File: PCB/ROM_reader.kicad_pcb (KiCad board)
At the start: 2 copper layers, 94 x 59 mm, 41 parts, among them J1 TTL_UART, J2 USB_B_Mini, J3 ISP, J4 DB25_Plug, M1 MountingHole_3.2mm_M3_DIN965, M2 MountingHole_3.2mm_M3_DIN965, M3 MountingHole_3.2mm_M3_DIN965, M4 MountingHole_3.2mm_M3_DIN965, SW1 RST, U1 CH340G, U2 ATmega128A-A, Y1 12MHz, Y2 12MHz

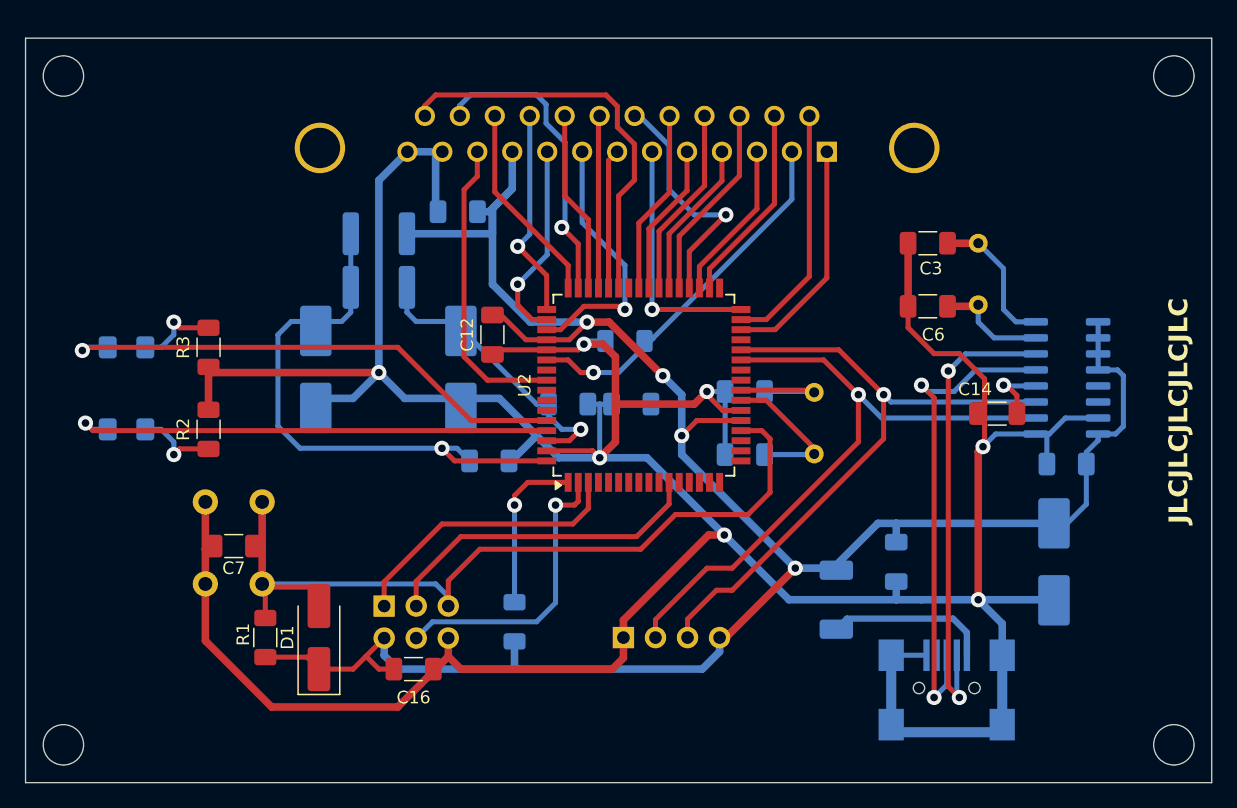
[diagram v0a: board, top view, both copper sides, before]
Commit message: ROM reader project PCBs updated
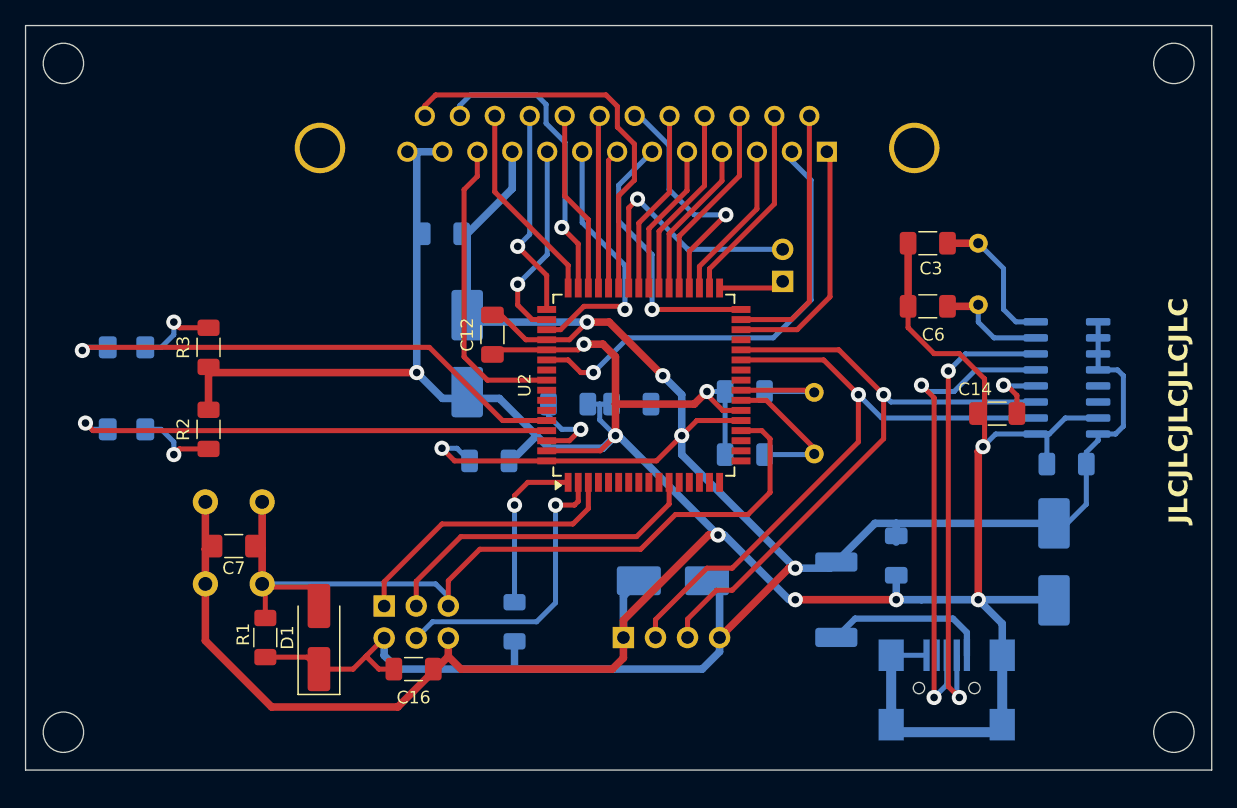
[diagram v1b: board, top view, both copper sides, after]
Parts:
- removed C11: 100u, Capacitor_SMD:CP_Elec_8x5.4
- removed L1, L2: 100u, Inductor_SMD:L_1812_4532Metric_Pad1.30x3.40mm_HandSolder
- removed M1, M2, M3, M4: MountingHole_3.2mm_M3_DIN965, MountingHole:MountingHole_3.2mm_M3_DIN965
- removed R5: 10M, Resistor_SMD:R_1206_3216Metric_Pad1.30x1.75mm_HandSolder
- added D5: Schottky, Diode_SMD:D_SMB_Handsoldering, B.Cu at (143.3, 104.5)
- added H1: MH, MountingHole:MountingHole_3.2mm_M3_DIN965, F.Cu at (95.0, 63.5)
- added H2: MH, MountingHole:MountingHole_3.2mm_M3_DIN965, F.Cu at (183.0, 63.5)
- added H3: MH, MountingHole:MountingHole_3.2mm_M3_DIN965, F.Cu at (183.0, 116.5)
- added H4: MH, MountingHole:MountingHole_3.2mm_M3_DIN965, F.Cu at (95.0, 116.5)
- added J4: EC, Connector_PinHeader_2.54mm:PinHeader_1x02_P2.54mm_Vertical, B.Cu at (152.0, 80.8)
- F1: footprint Fuse:Fuse_2010_5025Metric_Pad1.52x2.65mm_HandSolder -> Fuse:Fuse_2512_6332Metric_Pad1.52x3.35mm_HandSolder
- R2, R3: value 10k -> 1k5
- Y2: value 12MHz -> 7.3782MHz
- moved C8 12.1 mm to (127.0, 86.5)
- moved C4 2.15 mm to (125.0, 77.0)
- moved C9 0.50 mm to (161.0, 102.5)
- renumbered J2 to J1, J1 to J2, J4 to J5
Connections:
- C1 pad 1: +5V -> AVCC
- C12 pad 1: +5V -> AVCC
- C16 pad 1: +5V -> AVCC
- C17 pad 1: +5V -> AVCC
- C2 pad 1: +5V -> AVCC
- C4 pad 1: +5V -> AVCC
- C9 pad 1: +5V -> AVCC
- D1 pad 1: +5V -> AVCC
- F1 pad 2: +5V -> AVCC
- J2 pad 4: +5V -> AVCC
- J3 pad 2: +5V -> AVCC
- J5 pad 10: +5V -> AVCC
- R1 pad 2: +5V -> AVCC
- R4 pad 2: +5V -> AVCC
- U1 pad 10: +5V -> AVCC
- U1 pad 11: +5V -> AVCC
- U1 pad 12: +5V -> AVCC
- U1 pad 16: +5V -> AVCC
- U1 pad 9: +5V -> AVCC
- U2 pad 21: +5V -> AVCC
- U2 pad 33: unconnected-(U2-PG0-Pad33) -> #WR
- U2 pad 42: unconnected-(U2-PC7-Pad42) -> A15_RAM_ADAPTER
- U2 pad 52: +5V -> AVCC
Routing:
- net +5V: track 175.7 -> 0.00 mm, vias 4 -> 0
- net AVCC: track 45.0 -> 195.3 mm, vias 1 -> 5
- net A15_RAM_ADAPTER: track 0.00 -> 20.5 mm, vias 0 -> 1
- net AREF: track 23.2 -> 7.01 mm
- net GND: track 303.8 -> 294.1 mm, vias 7 -> 9
- net /A15: track 30.1 -> 36.1 mm
- net #WR: track 0.00 -> 5.22 mm
- net B+C: track 19.5 -> 21.7 mm
- net B: track 18.5 -> 19.7 mm
- net #A: track 19.5 -> 20.7 mm
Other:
- board text added: "EC"
- board text added: "FLT/ART/CU-1 ROM READER"
- board text added: "FUSE"

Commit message: Minor changes in text placement on PCB, comments. Revision updated to B
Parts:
- D3: renamed from D2; footprint LED_SMD:LED_1206_3216Metric_Pad1.42x1.75mm_HandSolder -> LED_SMD:LED_2010_5025Metric_Pad1.52x2.65mm_HandSolder
- D4: renamed from D3; footprint LED_SMD:LED_1206_3216Metric_Pad1.42x1.75mm_HandSolder -> LED_SMD:LED_2010_5025Metric_Pad1.52x2.65mm_HandSolder
- J4: value EC -> RAM ADAPTER EXT; footprint Connector_PinHeader_2.54mm:PinHeader_1x02_P2.54mm_Vertical -> Connector_PinHeader_2.54mm:PinHeader_1x02_P2.54mm_Horizontal
- J5: value DB25_Plug -> ROM MODULE
- moved J4 24.3 mm to (175.3, 73.9), turned to 90 degrees
- renumbered C12 to C11, C13 to C12, C14 to C13, C15 to C14, C16 to C15, C17 to C16, D5 to D1, D1 to D2, H3 to H2, H2 to H3
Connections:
- net AVCC renamed +5V
- J5 pad 0: (no net) -> GND
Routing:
- net #WR: track 5.22 -> 44.6 mm, vias 0 -> 2
- net A15_RAM_ADAPTER: track 20.5 -> 57.5 mm
- net GND: track 294.1 -> 301.1 mm
- net /A9: track 19.5 -> 17.0 mm
- net Net-(D3-K): track 6.61 -> 5.86 mm
- net Net-(D4-K): track 6.61 -> 5.91 mm
- net Net-(D3-A): track 38.8 -> 39.4 mm
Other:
- board text added: "ADAPTER"
- board text added: "MODULE"
- board text added: "RAM"
- board text added: "ROM"
- board text added: "trwgQ26xxx"
- board text removed: "EC"

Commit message: PCB project update: pull-up resistors added for D0-D7 data lines
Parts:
- added R10: 22k, Resistor_SMD:R_1206_3216Metric_Pad1.30x1.75mm_HandSolder, F.Cu at (134.4, 75.3)
- added R11: 22k, Resistor_SMD:R_1206_3216Metric_Pad1.30x1.75mm_HandSolder, F.Cu at (134.8, 73.0)
- added R12: 22k, Resistor_SMD:R_1206_3216Metric_Pad1.30x1.75mm_HandSolder, B.Cu at (137.8, 78.2)
- added R5: 22k, Resistor_SMD:R_1206_3216Metric_Pad1.30x1.75mm_HandSolder, B.Cu at (137.8, 80.6)
- added R6: 22k, Resistor_SMD:R_1206_3216Metric_Pad1.30x1.75mm_HandSolder, B.Cu at (133.4, 81.4)
- added R7: 22k, Resistor_SMD:R_1206_3216Metric_Pad1.30x1.75mm_HandSolder, B.Cu at (129.2, 78.4)
- added R8: 22k, Resistor_SMD:R_1206_3216Metric_Pad1.30x1.75mm_HandSolder, F.Cu at (129.0, 78.3)
- added R9: 22k, Resistor_SMD:R_1206_3216Metric_Pad1.30x1.75mm_HandSolder, F.Cu at (124.8, 73.0)
- R2, R3: value 1k5 -> 2k2
- Y2: value 7.3782MHz -> 7.3728MHz
- renumbered C12 to C10, C14 to C11, C13 to C12, C4 to C13, C15 to C14, C16 to C15, C11 to C16, C5 to C4, C7 to C5, C8 to C7, C9 to C8, C10 to C9
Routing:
- net +5V: track 195.3 -> 220.2 mm, vias 5 -> 7
- net /D7: track 11.1 -> 19.1 mm
- net /D4: track 24.1 -> 29.5 mm
- net /D2: track 16.7 -> 19.1 mm
- net /D3: track 16.0 -> 18.3 mm
- net A15_RAM_ADAPTER: track 57.5 -> 59.1 mm
- net GND: track 301.1 -> 300.0 mm, vias 9 -> 8
- net /D6: track 13.7 -> 14.7 mm
- net /D1: track 15.9 -> 16.7 mm
- net B+C: track 21.7 -> 20.9 mm

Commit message: Minor updates
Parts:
- C1, C7: footprint Capacitor_SMD:CP_Elec_8x5.4 -> Capacitor_SMD:CP_Elec_6.3x7.7
- D3, D4: footprint LED_SMD:LED_2010_5025Metric_Pad1.52x2.65mm_HandSolder -> LED_SMD:LED_1206_3216Metric_Pad1.42x1.75mm_HandSolder
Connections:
- J4 pad 1: #WR -> A15_RAM_ADAPTER
- J4 pad 2: A15_RAM_ADAPTER -> #WR
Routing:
- net #WR: track 44.6 -> 42.5 mm, vias 2 -> 1
- net GND: track 300.0 -> 301.1 mm
- net A15_RAM_ADAPTER: track 59.1 -> 59.8 mm
